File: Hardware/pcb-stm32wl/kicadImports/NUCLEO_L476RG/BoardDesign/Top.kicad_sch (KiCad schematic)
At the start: 17 parts, among them T1 TRANS_P-CHANNEL_STS9P3LLH6, U10 LD39050PU33R, U4 LD1117S50TR

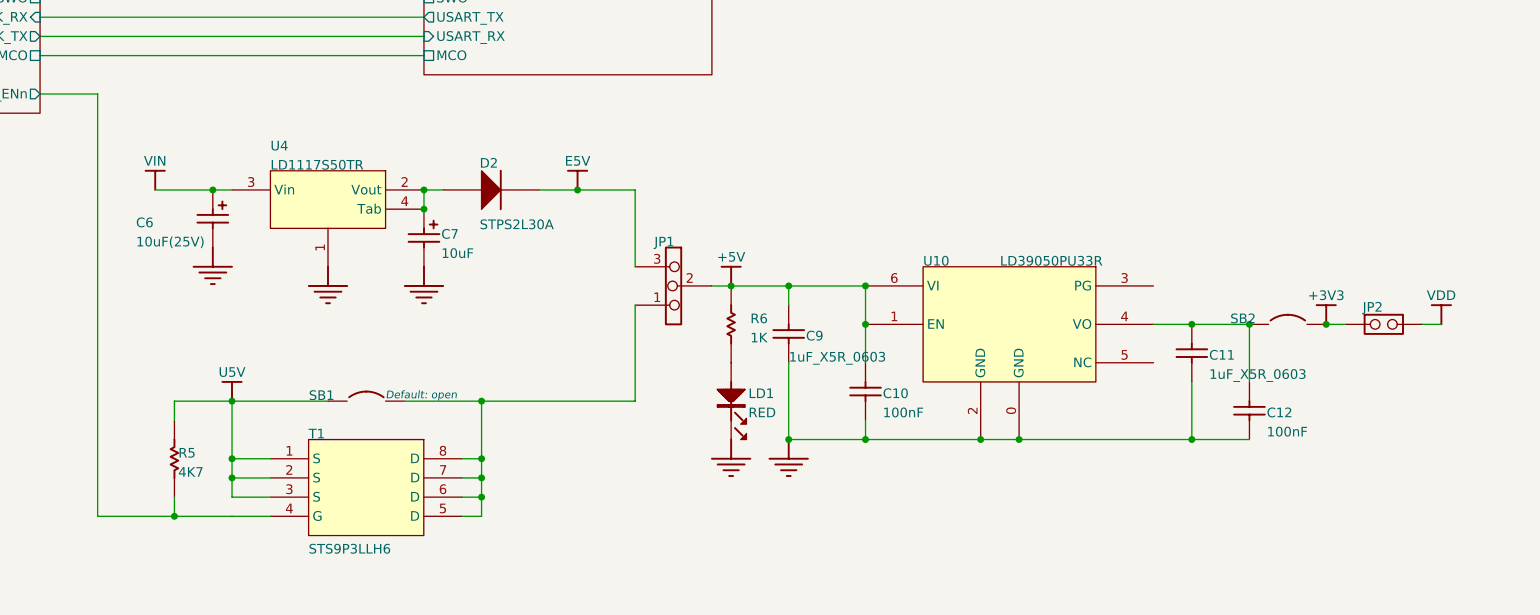
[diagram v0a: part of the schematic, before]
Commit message: . Re-imported NUCLEO_L476RG/BoardDesign/* files using KiCad 9.0.0 one at a time (to avoid a bug evident in misconnections in MCU_64), copied the schematic contents into local kicad_sch files with the same names, prefixed with NUCLEO_L476RG_*
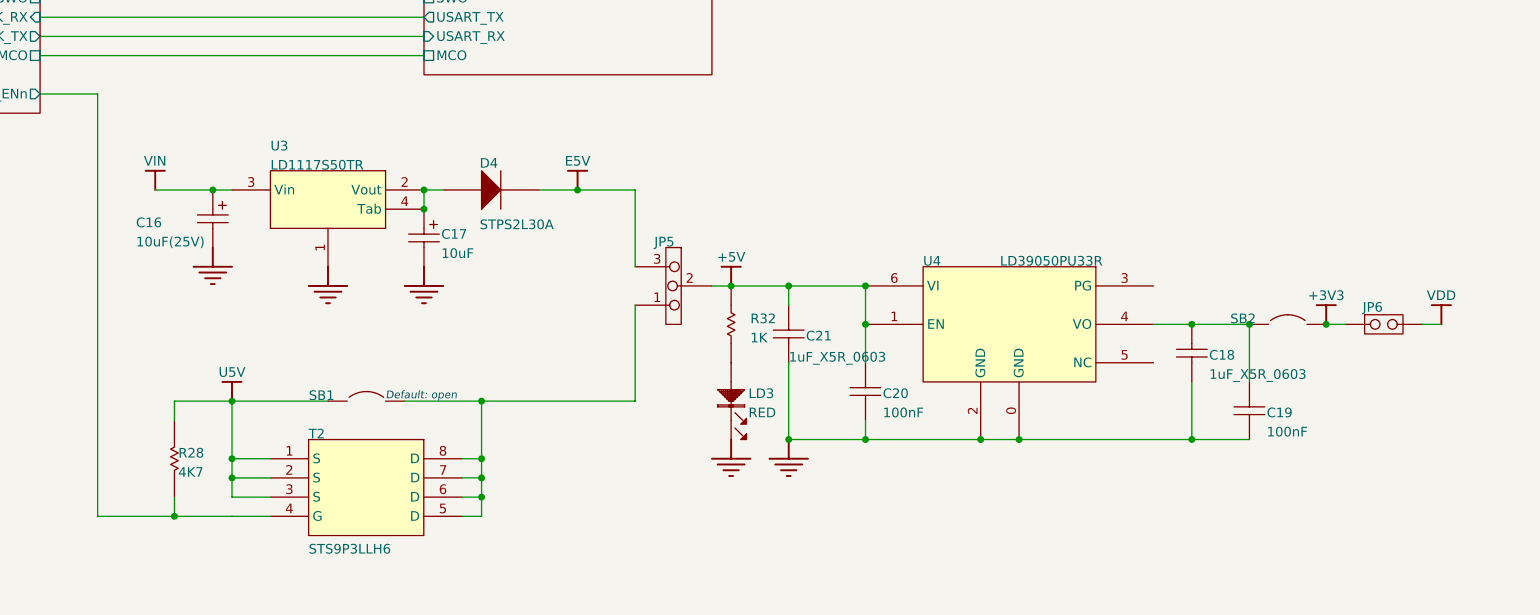
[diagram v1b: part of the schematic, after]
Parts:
- removed C10, C12: 100nF, 0603C, symbol Project_Overview-altium-import:U_Top_1_Capacitor_ST
- removed C11, C9: 1uF_X5R_0603, 0603C, symbol Project_Overview-altium-import:U_Top_3_CAP SMD 0603 X5R 1µF 25V 10%
- removed C6: 10uF(25V), TAN-B, symbol Project_Overview-altium-import:U_Top_3_Cap Pol1
- removed C7: 10uF, TAN-A, symbol Project_Overview-altium-import:U_Top_3_Cap Pol1
- removed D2: STPS2L30A, SMA, symbol Project_Overview-altium-import:U_Top_0_STPS2L30A
- removed JP1: ~, SIP3, symbol Project_Overview-altium-import:U_Top_0_Jumper3
- removed JP2: ~, SIP2/2.54, symbol Project_Overview-altium-import:U_Top_0_JP2
- removed LD1: RED, 0603D, symbol Project_Overview-altium-import:U_Top_0_PHOTO_0
- removed R5: 4K7, 0603R, symbol Project_Overview-altium-import:U_Top_1_mirrored_Res1_0
- removed R6: 1K, 0603R, symbol Project_Overview-altium-import:U_Top_1_Resistor_ST
- removed SB1, SB2: Circuit Breaker, JP2_SMD, symbol Project_Overview-altium-import:U_Top_0_Circuit Breaker
- removed T1: TRANS_P-CHANNEL_STS9P3LLH6, ICC_SO8_5X4_P127, symbol Project_Overview-altium-import:U_Top_0_TRANS_P-CHANNEL_STS9P3LLH6
- removed U10: LD39050PU33R, DFN6(3X3), symbol Project_Overview-altium-import:U_Top_0_LD39050P_0
- removed U4: LD1117S50TR, SOT-223, symbol Project_Overview-altium-import:U_Top_0_LD1117_0
- added C16: 10uF(25V), TAN-B, symbol Top-altium-import:root_3_Cap Pol1_Miscellaneous Devices.IntLib
- added C17: 10uF, TAN-A, symbol Top-altium-import:root_3_Cap Pol1_Miscellaneous Devices.IntLib
- added C18, C21: 1uF_X5R_0603, 0603C, symbol Top-altium-import:root_3_CAP SMD 0603 X5R 1µF 25V 10%_MB963_1.SCHLIB
- added C19, C20: 100nF, 0603C, symbol Top-altium-import:root_1_Capacitor_ST_MCD_TOOLS.SchLib
- added D4: STPS2L30A, SMA, symbol Top-altium-import:root_0_STPS2L30A_Nucleo_64.SCHLIB
- added JP5: (no value), SIP3, symbol Top-altium-import:root_0_Jumper3_STR910_SCHLIB.SCHLIB
- added JP6: (no value), SIP2/2.54, symbol Top-altium-import:root_0_JP2_*
- added LD3: RED, 0603D, symbol Top-altium-import:root_0_PHOTO_MB963_1.SCHLIB_0
- added R28: 4K7, 0603R, symbol Top-altium-import:root_1_mirrored_Res1_*_0
- added R32: 1K, 0603R, symbol Top-altium-import:root_1_Resistor_ST_MCD_TOOLS.SchLib
- added SB1, SB2: Circuit Breaker, JP2_SMD, symbol Top-altium-import:root_0_Circuit Breaker_MCD_TOOLS.SCHLIB
- added T2: TRANS_P-CHANNEL_STS9P3LLH6, ICC_SO8_5X4_P127, symbol Top-altium-import:root_0_TRANS_P-CHANNEL_STS9P3LLH6_MCD_PARTS_database.DbLib
- added U3: LD1117S50TR, SOT-223, symbol Top-altium-import:root_0_LD1117_mb1045.SCHLIB_0
- added U4: LD39050PU33R, DFN6(3X3), symbol Top-altium-import:root_0_LD39050P_Nucleo_64.SCHLIB_0
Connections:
- net +3V3: now also JP6.1 (COMMON), SB2.2
- net +5V: now also C20.2, C21.1, JP5.2, R32.2, U4.1 (EN), U4.6 (VI)
- net E5V: now also D4.2 (K), JP5.3
- net GND: now also C16.2, C17.2, C18.2, C19.1, C20.1, C21.2, LD3.2, U3.1, U4.0 (GND), U4.2 (GND)
- net U5V: now also R28.1, SB1.1, T2.1 (S), T2.2 (S), T2.3 (S)
- net U_ST_LINK_V2-1/PWR_ENn: now also R28.2, T2.4 (G)
- net VDD: now also JP6.2 (NO)
- net VIN: now also C16.1, U3.3 (Vin)
- new net: JP5.1, SB1.2, T2.5 (D), T2.6 (D), T2.7 (D), T2.8 (D)
- new net: LD3.1, R32.1
- new net: C17.1, D4.1 (A), U3.2 (Vout), U3.4 (Tab)
- new net: C18.1, C19.2, SB2.1, U4.4 (VO)
